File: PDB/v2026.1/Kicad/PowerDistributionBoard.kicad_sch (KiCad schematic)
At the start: 77 parts, among them J1 Conn_02x01_12V_EXP3, J10 Conn_02x02_BMS, J11 Conn_02x02_IMD, J12 Conn_02x02_Suspension_Linear_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, J13 Conn_02x02_Suspension_Linear_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, J14 Conn_02x02_Suspension_Linear_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, J15 Conn_02x02_Suspension_Linear_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, J16 Conn_02x05_CCM_Faults, J17 EXP1_5V, J18 RasPI_5V, J19 LATCH_12V, J2 Conn_02x01_12V_EXP2, J20 Throttle_Sensor, J21 Conn_02x02_Current_Sensor, J22 Conn_02x02_Brake_Sensor1, J23 Conn_02x02_Brake_Sensor2, J24 Conn_02x02_Wheel_Sensor1, J25 Conn_02x02_Wheel_Sensor2, J26 Conn_02x01_3V_EXP, J27 BATTERY_12V, J28 BATTERY_GND, J29 BATTERY_24V, J3 Conn_02x01_12V_EXP, J31 FAN1_24V, J32 FAN2_24V, J33 PUMP1_24V, J34 PUMP2_24V, J35 24V_EXP1, J4 Conn_02x01_RTM, J5 CCM_12V, J7 Conn_02x02_BSPD, J8 Conn_02x02_LATCH, J9 Conn_02x02_TSSI, U1 5to3.3_Linear_Regulator, U2 TLV76150DCYR

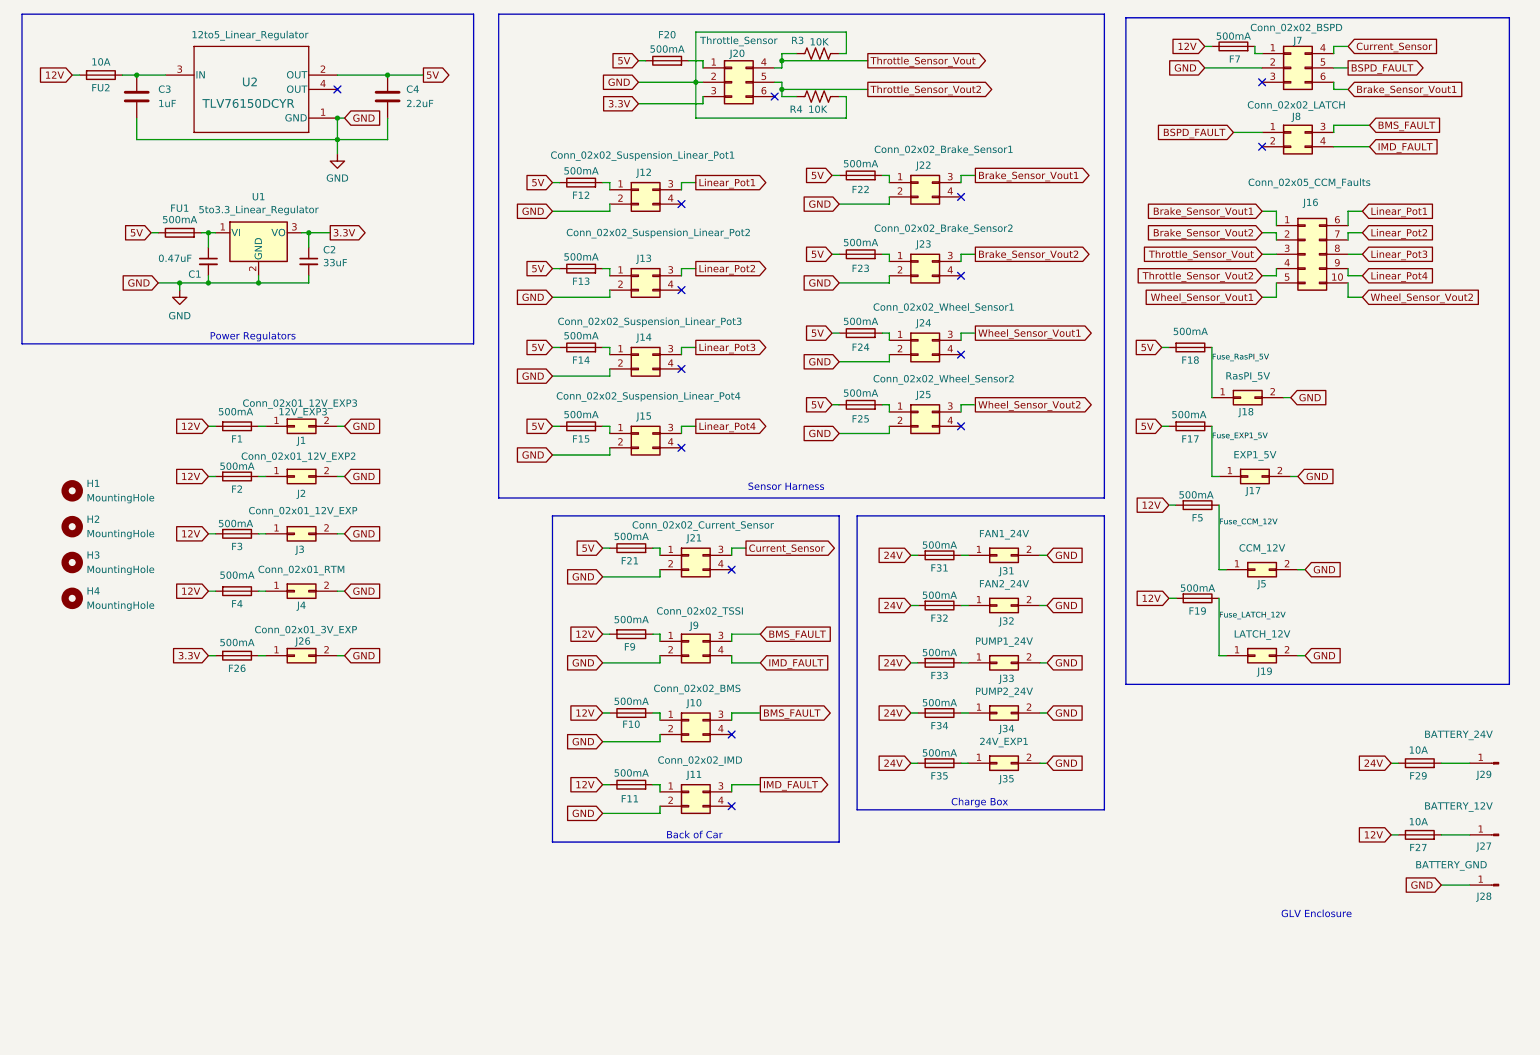
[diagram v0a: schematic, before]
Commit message: Silkscreen pin assignment now easier
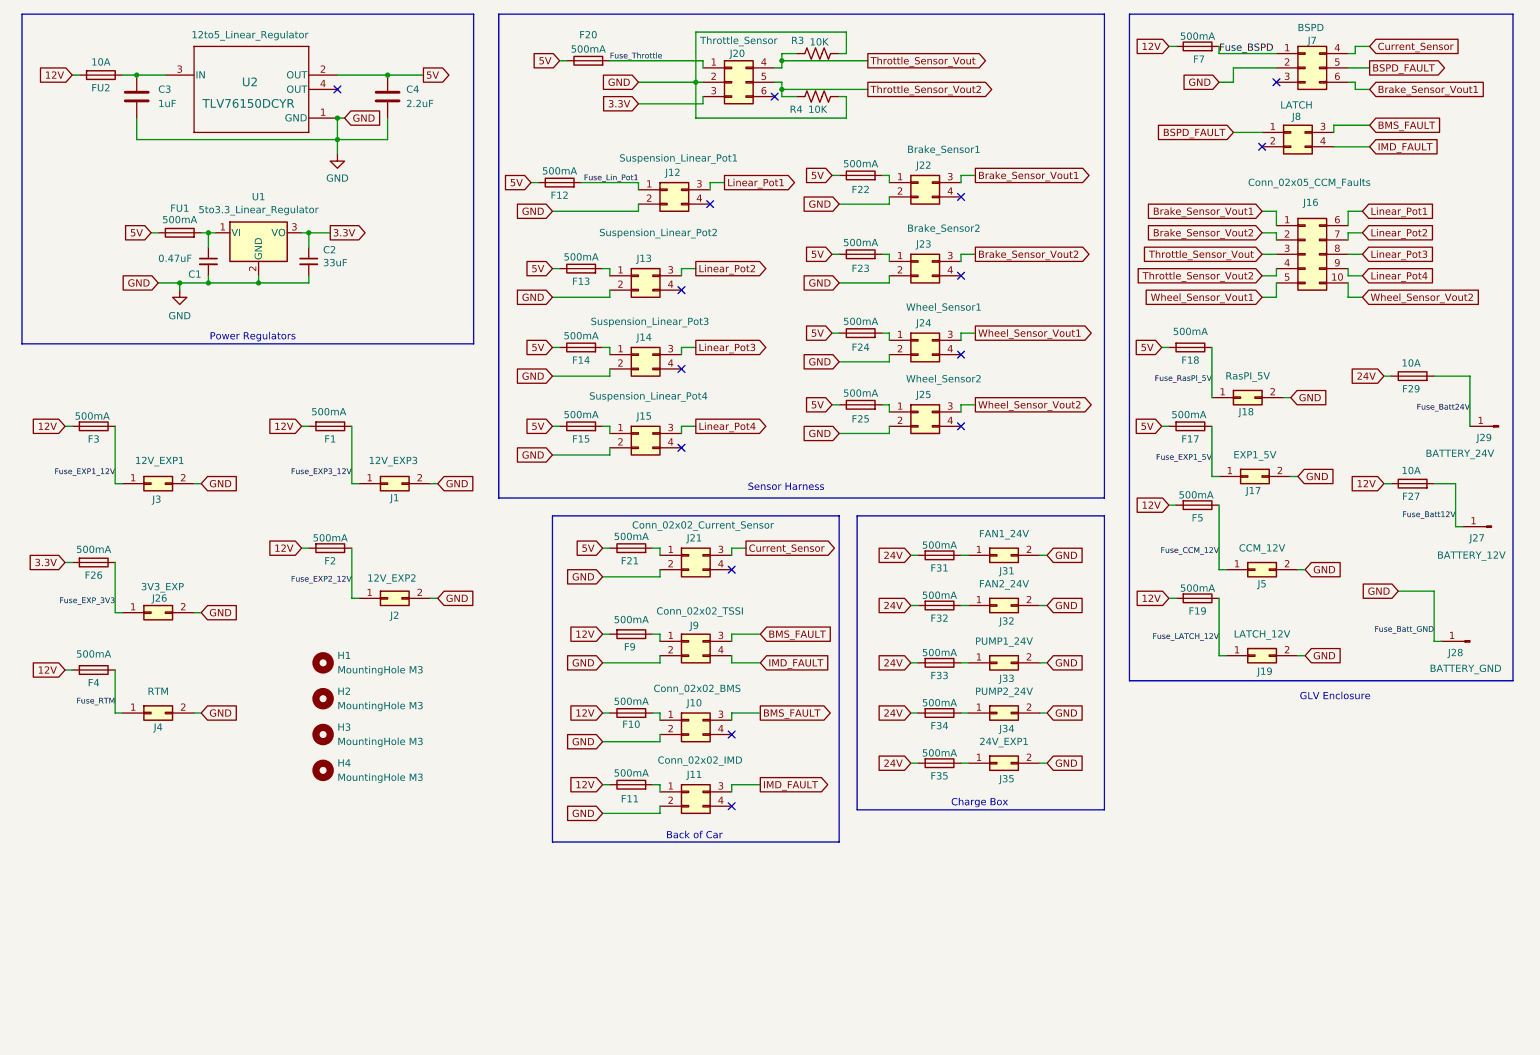
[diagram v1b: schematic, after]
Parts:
- H1, H2, H3, H4: value MountingHole -> MountingHole M3
- J1: value Conn_02x01_12V_EXP3 -> 12V_EXP3
- J12: value Conn_02x02_Suspension_Linear_Pot1 -> Suspension_Linear_Pot1
- J13: value Conn_02x02_Suspension_Linear_Pot2 -> Suspension_Linear_Pot2
- J14: value Conn_02x02_Suspension_Linear_Pot3 -> Suspension_Linear_Pot3
- J15: value Conn_02x02_Suspension_Linear_Pot4 -> Suspension_Linear_Pot4
- J2: value Conn_02x01_12V_EXP2 -> 12V_EXP2
- J22: value Conn_02x02_Brake_Sensor1 -> Brake_Sensor1
- J23: value Conn_02x02_Brake_Sensor2 -> Brake_Sensor2
- J24: value Conn_02x02_Wheel_Sensor1 -> Wheel_Sensor1
- J25: value Conn_02x02_Wheel_Sensor2 -> Wheel_Sensor2
- J26: value Conn_02x01_3V_EXP -> 3V3_EXP
- J3: value Conn_02x01_12V_EXP -> 12V_EXP1
- J4: value Conn_02x01_RTM -> RTM
- J7: value Conn_02x02_BSPD -> BSPD
- J8: value Conn_02x02_LATCH -> LATCH
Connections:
- net Fuse_EXP1_12V: now reaches F3.1, J3.1 (Pin_1)
- net Fuse_EXP_3V3: now reaches F26.1, J26.1 (Pin_1)
- net Fuse_EXP3_12V: now reaches F1.1, J1.1 (Pin_1)
- net Fuse_EXP2_12V: now reaches F2.1, J2.1 (Pin_1)
- net Fuse_Lin_Pot1: now reaches F12.2, J12.1 (Pin_1)
- net Fuse_Batt24V: now reaches F29.2, J29.1 (Pin_1)
- net Fuse_Batt12V: now reaches F27.2, J27.1 (Pin_1)
- net Fuse_BSPD: now reaches F7.2, J7.1 (Pin_1)
- net Fuse_Throttle: now reaches F20.2, J20.1 (Pin_1)
- net Fuse_RTM: now reaches F4.1, J4.1 (Pin_1)
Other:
- moved on the sheet: F1, F12, F2, F20, F26, F27, F29, F3, F4, F7, H1, H2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

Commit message: Restored step files
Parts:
- J16: footprint Connector_Molex:Molex_Mini-Fit_Jr_5566-10A_2x05_P4.20mm_Vertical -> 0footprints:Molex_Mini-Fit_Jr_5566-10A_2x05_P4.20mm_Vertical
- J20, J7: footprint Connector_Molex:Molex_Mini-Fit_Jr_5566-06A_2x03_P4.20mm_Vertical -> 0footprints:Molex_Mini-Fit_Jr_5566-06A_2x03_P4.20mm_Vertical
- J27, J28, J29: footprint TerminalBlock:KEYSTONE_7797 -> 0footprints:KEYSTONE_7797
- U2: footprint Converter_DCDC:DCY0004A-IPC_A -> Package_TO_SOT_SMD:SOT-223
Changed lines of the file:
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@@
 			)
 		)
-		(property "Footprint" "Converter_DCDC:DCY0004A-IPC_A"
+		(property "Footprint" "Package_TO_SOT_SMD:SOT-223"
 			(at 41.91 24.13 0)
 			(effects
@@
 			)
 		)
-		(property "Footprint" "TerminalBlock:KEYSTONE_7797"
+		(property "Footprint" "0footprints:KEYSTONE_7797"
 			(at 276.86 87.63 0)
 			(effects
@@
 			)
 		)
-		(property "Footprint" "TerminalBlock:KEYSTONE_7797"
+		(property "Footprint" "0footprints:KEYSTONE_7797"
 			(at 275.59 105.41 0)
 			(effects
@@
 			)
 		)
-		(property "Footprint" "Connector_Molex:Molex_Mini-Fit_Jr_5566-06A_2x03_P4.20mm_Vertical"
+		(property "Footprint" "0footprints:Molex_Mini-Fit_Jr_5566-06A_2x03_P4.20mm_Vertical"
 			(at 140.97 26.67 0)
 			(effects
@@
 			)
 		)
-		(property "Footprint" "Connector_Molex:Molex_Mini-Fit_Jr_5566-06A_2x03_P4.20mm_Vertical"
+		(property "Footprint" "0footprints:Molex_Mini-Fit_Jr_5566-06A_2x03_P4.20mm_Vertical"
 			(at 242.57 24.13 0)
 			(effects
@@
 			)
 		)
-		(property "Footprint" "TerminalBlock:KEYSTONE_7797"
+		(property "Footprint" "0footprints:KEYSTONE_7797"
 			(at 271.78 125.73 0)
 			(effects
@@
 			)
 		)
-		(property "Footprint" "Connector_Molex:Molex_Mini-Fit_Jr_5566-10A_2x05_P4.20mm_Vertical"
+		(property "Footprint" "0footprints:Molex_Mini-Fit_Jr_5566-10A_2x05_P4.20mm_Vertical"
 			(at 242.57 57.15 0)
 			(effects

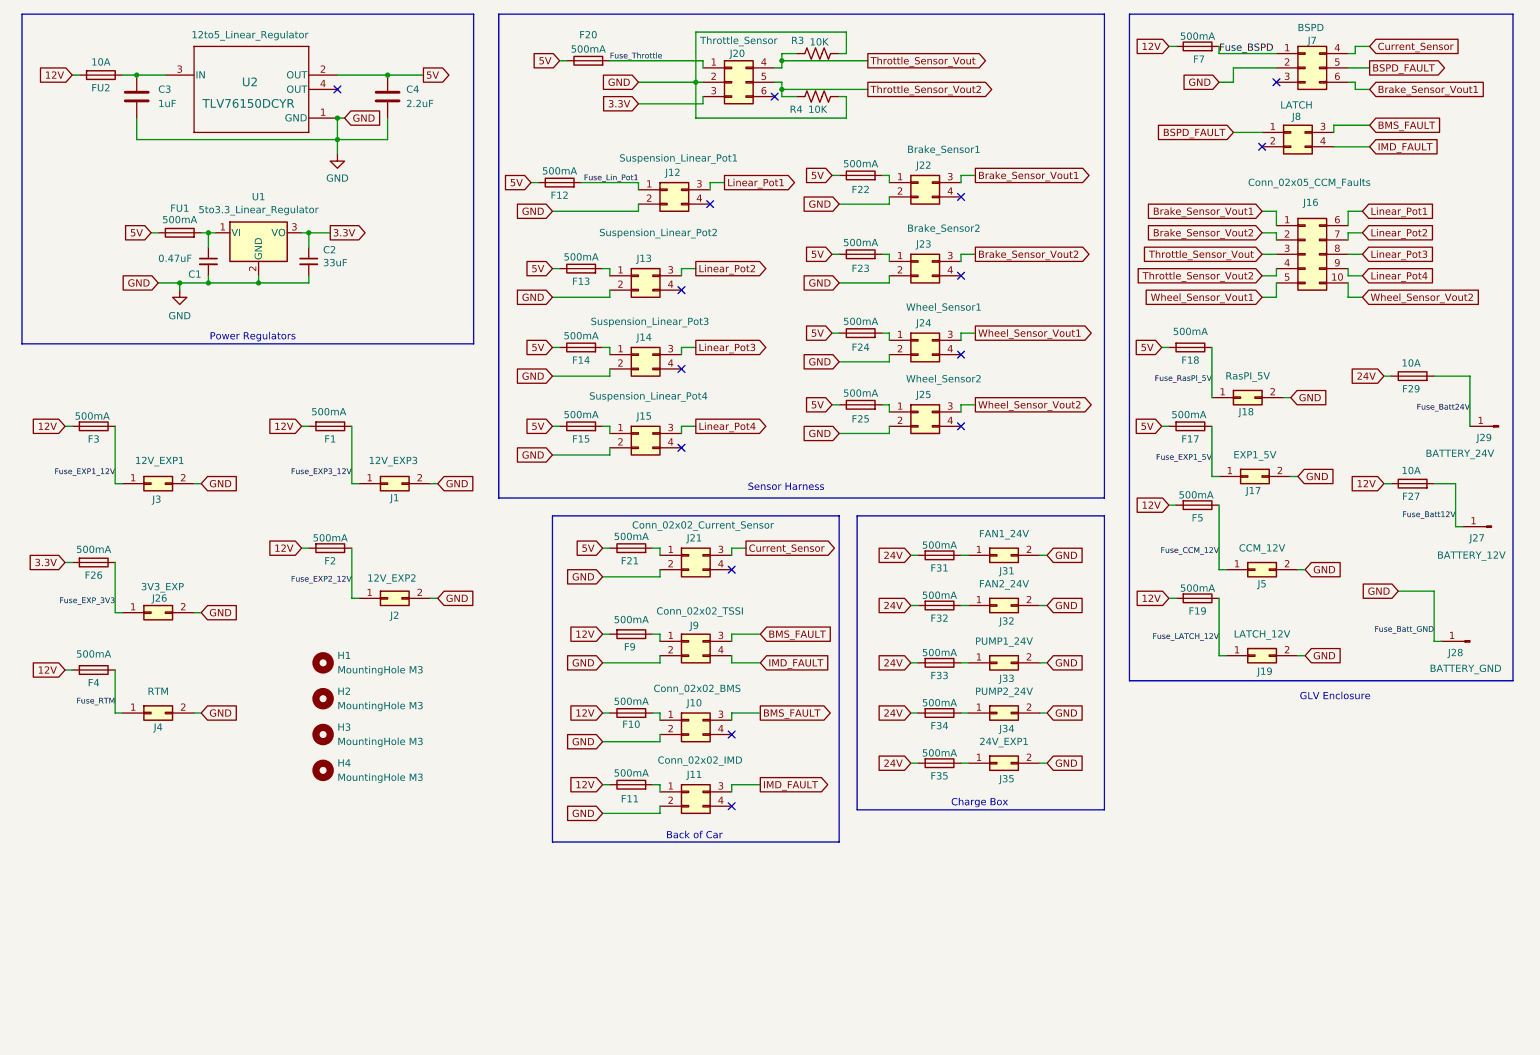
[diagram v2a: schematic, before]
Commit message: Updated throttle sensors, marked 24V components DNP
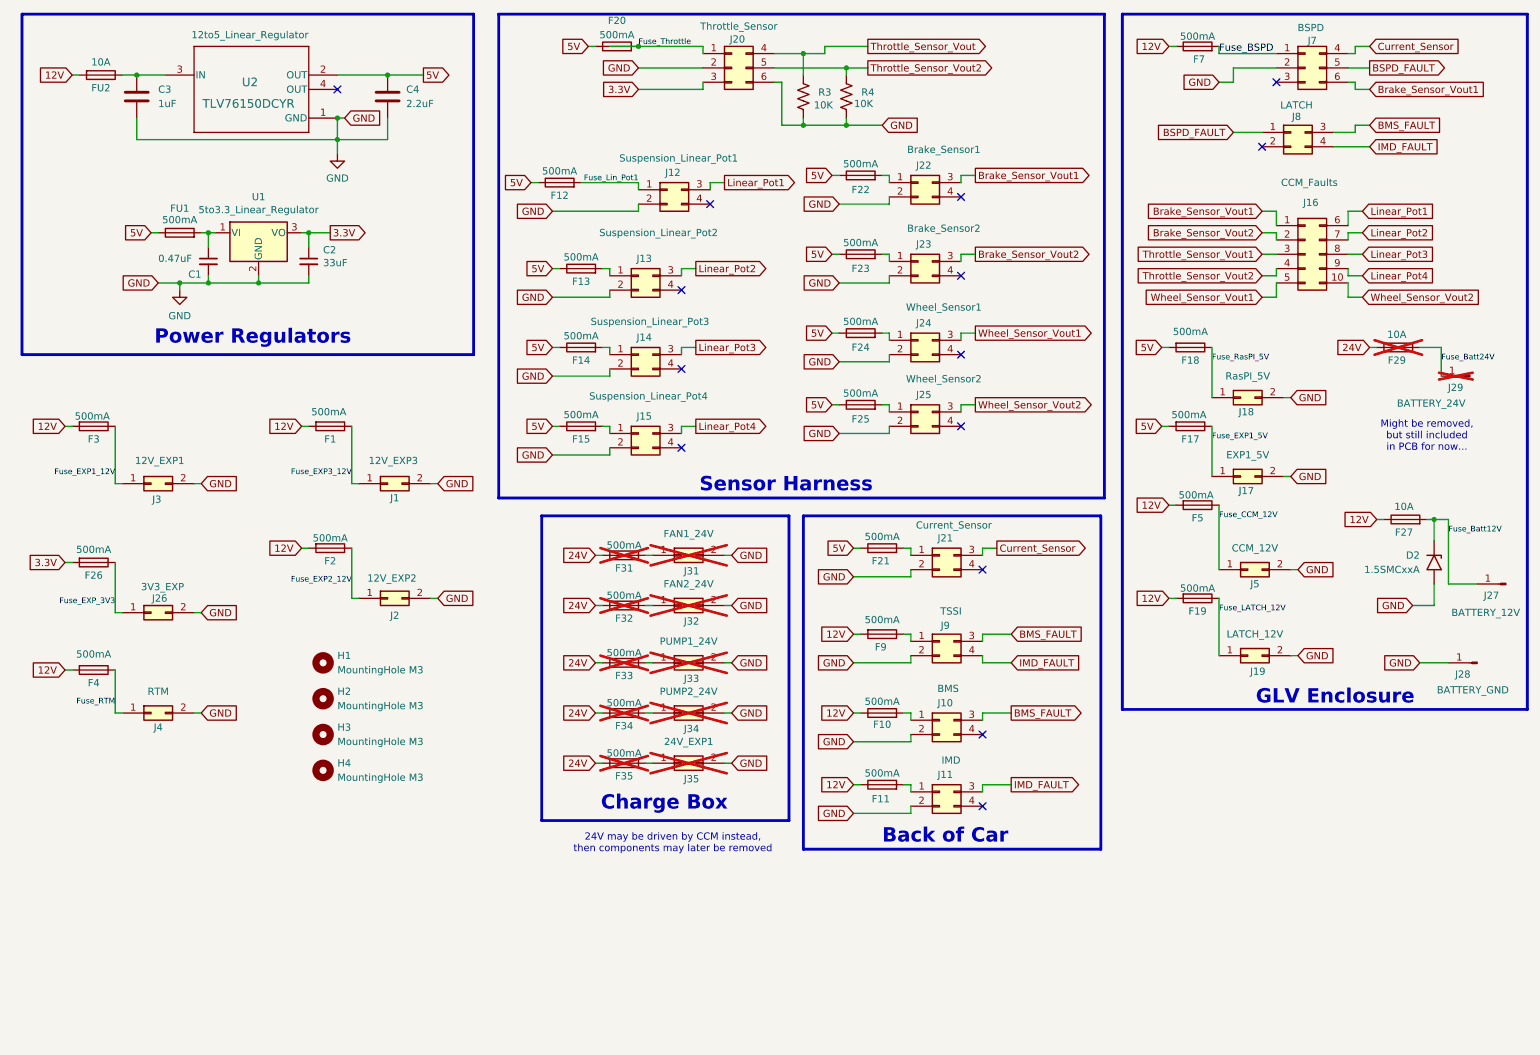
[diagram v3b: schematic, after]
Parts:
- added D2: 1.5SMCxxA, Diode_SMD:D_SMC, symbol Diode:1.5SMCxxA
- F29, F31, F32, F33, F34, F35, J29, J31, J32, J33, J34, J35: now not fitted
- J10: value Conn_02x02_BMS -> BMS
- J11: value Conn_02x02_IMD -> IMD
- J16: value Conn_02x05_CCM_Faults -> CCM_Faults
- J21: value Conn_02x02_Current_Sensor -> Current_Sensor
- J9: value Conn_02x02_TSSI -> TSSI
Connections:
- net Fuse_Batt12V: now also D2.1 (A1)
- net GND: now also J20.6 (Pin_6), D2.2 (A2)
- net Throttle_Sensor_Vout: no longer J16.3 (Pin_3)
- new net Throttle_Sensor_Vout1: J16.3 (Pin_3)
- no-connect marks 15 -> 14
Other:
- note added: "24V may be driven by CCM instead, then components may later be removed"
- note added: "Might be removed, but still included in PCB for now..."
- moved on the sheet: F10, F11, F20, F21, F27, F9, J10, J11, J17, J19, J20, J21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

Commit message: Added labels for every net
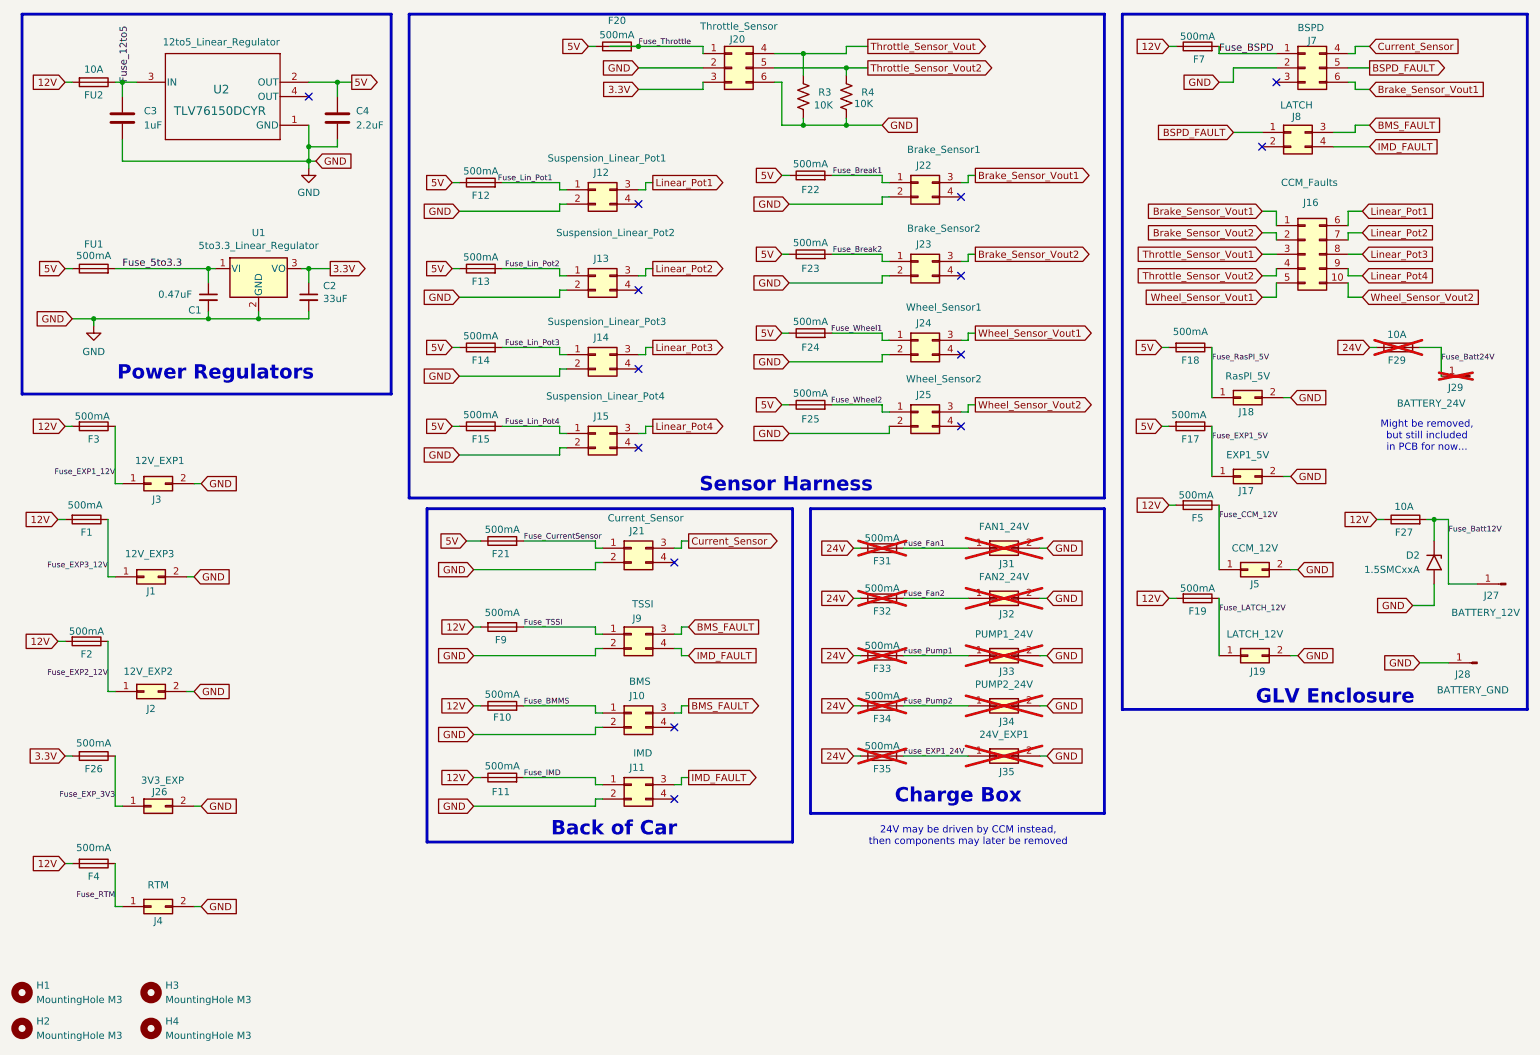
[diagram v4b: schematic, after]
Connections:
- net Fuse_EXP1_24V: now reaches F35.1, J35.1 (Pin_1)
- net Fuse_12to5: now reaches C3.1, FU2.1, U2.3 (IN)
- net Fuse_Wheel2: now reaches F25.2, J25.1 (Pin_1)
- net Fuse_Pump1: now reaches F33.1, J33.1 (Pin_1)
- net Fuse_5to3.3: now reaches C1.1, FU1.2, U1.1 (VI)
- net Fuse_BMMS: now reaches F10.2, J10.1 (Pin_1)
- net Fuse_Fan2: now reaches F32.1, J32.1 (Pin_1)
- net Fuse_Break1: now reaches F22.2, J22.1 (Pin_1)
- net Fuse_Wheel1: now reaches F24.2, J24.1 (Pin_1)
- net Fuse_IMD: now reaches F11.2, J11.1 (Pin_1)
- net Fuse_Pump2: now reaches F34.1, J34.1 (Pin_1)
- net Fuse_TSSI: now reaches F9.1, J9.1 (Pin_1)
- net Fuse_Lin_Pot3: now reaches F14.2, J14.1 (Pin_1)
- net Fuse_Break2: now reaches F23.2, J23.1 (Pin_1)
- net Fuse_Lin_Pot2: now reaches F13.2, J13.1 (Pin_1)
- net Fuse_Fan1: now reaches F31.1, J31.1 (Pin_1)
- net Fuse_CurrentSensor: now reaches F21.2, J21.1 (Pin_1)
- net Fuse_Lin_Pot4: now reaches F15.2, J15.1 (Pin_1)
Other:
- moved on the sheet: C1, C2, C3, C4, F1, F10, F11, F12, F13, F14, F15, F2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
